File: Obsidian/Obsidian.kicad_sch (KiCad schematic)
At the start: 5 parts

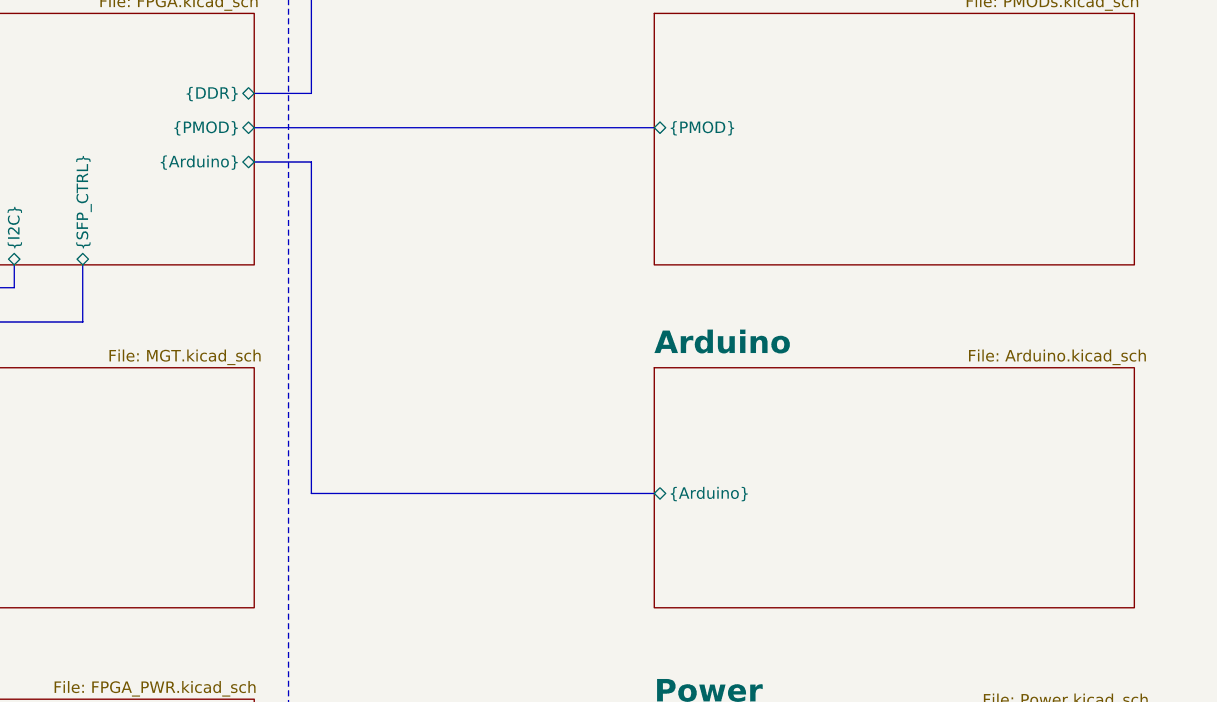
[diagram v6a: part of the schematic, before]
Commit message: adding flex connector
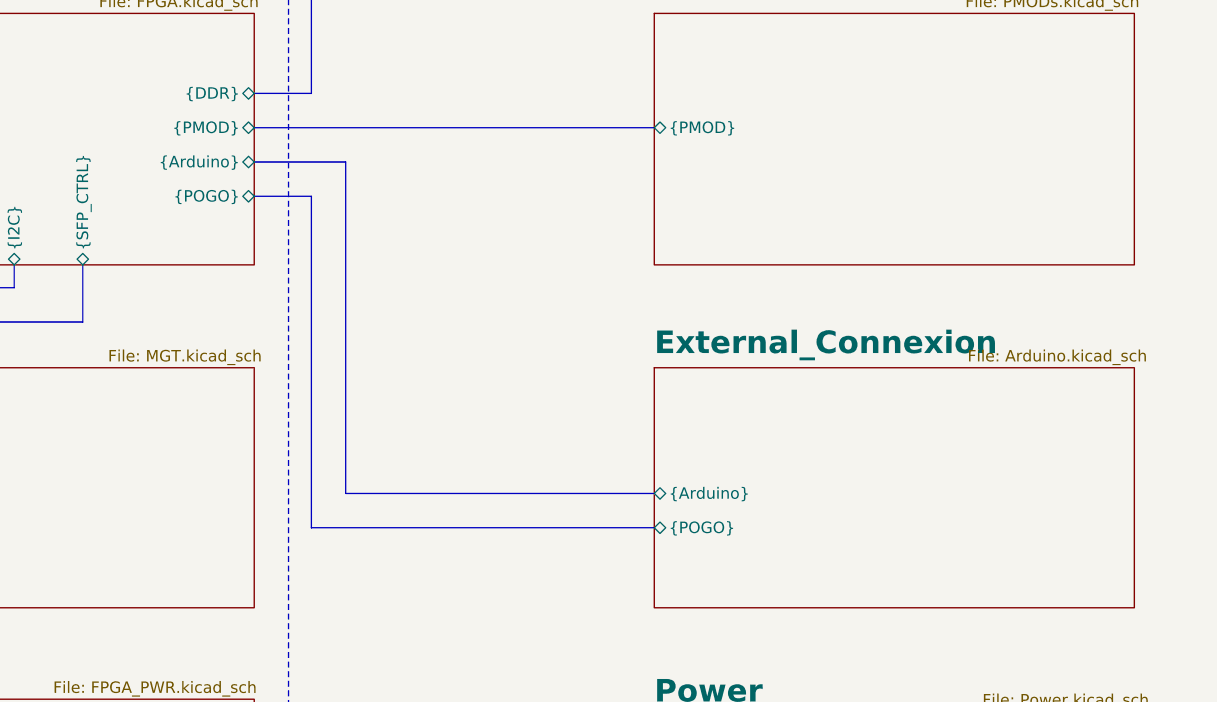
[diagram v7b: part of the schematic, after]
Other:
- sheet Arduino renamed External_Connexion
- sheet External_Connexion ports: added {POGO}; removed none
- sheet FPGA ports: added {POGO}; removed none
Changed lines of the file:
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@@
 	(bus
 		(pts
-			(xy 179.07 110.49) (xy 217.17 110.49)
+			(xy 182.88 110.49) (xy 217.17 110.49)
 		)
 		(stroke
@@
 	(bus
 		(pts
+			(xy 179.07 77.47) (xy 172.72 77.47)
+		)
+		(stroke
+			(width 0)
+			(type default)
+		)
+	)
+	(bus
+		(pts
+			(xy 217.17 114.3) (xy 179.07 114.3)
+		)
+		(stroke
+			(width 0)
+			(type default)
+		)
+	)
+	(bus
+		(pts
 			(xy 114.3 34.29) (xy 114.3 60.96)
 		)
@@
 	(bus
 		(pts
-			(xy 172.72 73.66) (xy 179.07 73.66)
+			(xy 172.72 73.66) (xy 182.88 73.66)
 		)
 		(stroke
@@
 	(bus
 		(pts
-			(xy 179.07 73.66) (xy 179.07 110.49)
+			(xy 182.88 73.66) (xy 182.88 110.49)
 		)
 		(stroke
@@
 		(pts
 			(xy 179.07 31.75) (xy 179.07 66.04)
+		)
+		(stroke
+			(width 0)
+			(type default)
+		)
+	)
+	(bus
+		(pts
+			(xy 179.07 114.3) (xy 179.07 77.47)
 		)
 		(stroke
@@
 			)
 		)
+		(pin "{POGO}" bidirectional
+			(at 172.72 77.47 0)
+			(effects
+				(font
+					(size 1.27 1.27)
+				)
+				(justify right)
+			)
+		)
 		(instances
 			(project "Obsidian"
@@
 			(color 128 255 128 1.0000)
 		)
-		(property "Sheetname" "Arduino"
+		(property "Sheetname" "External_Connexion"
 			(at 217.17 95.1934 0)
 			(effects
@@
 			(effects
 				(font
+					(size 1.27 1.27)
+				)
+				(justify left)
+			)
+		)
+		(pin "{POGO}" bidirectional
+			(at 217.17 114.3 180)
+			(effects
+				(font

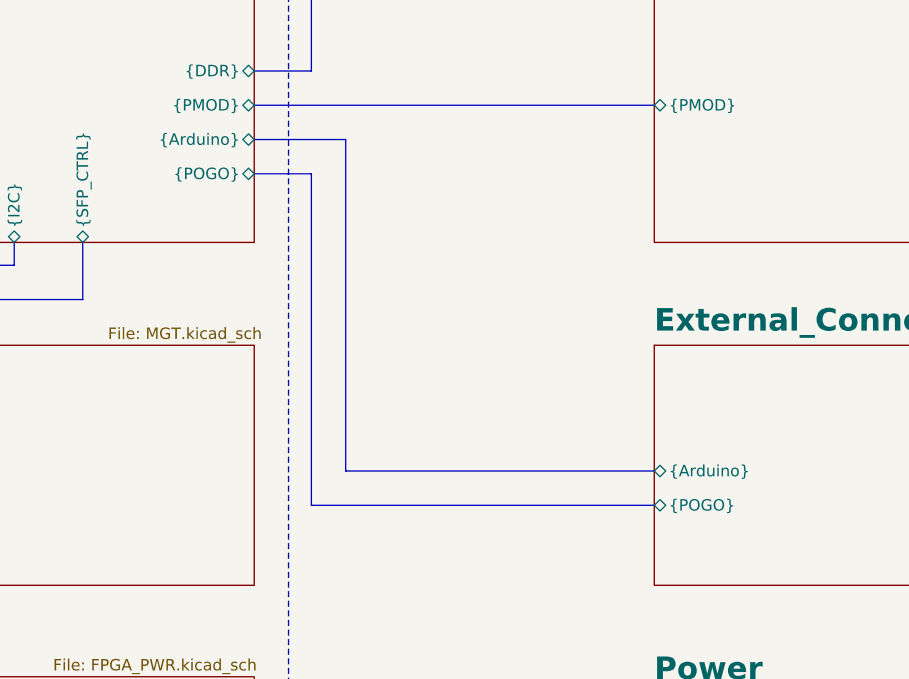
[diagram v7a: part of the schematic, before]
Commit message: Cleanup of the schematic
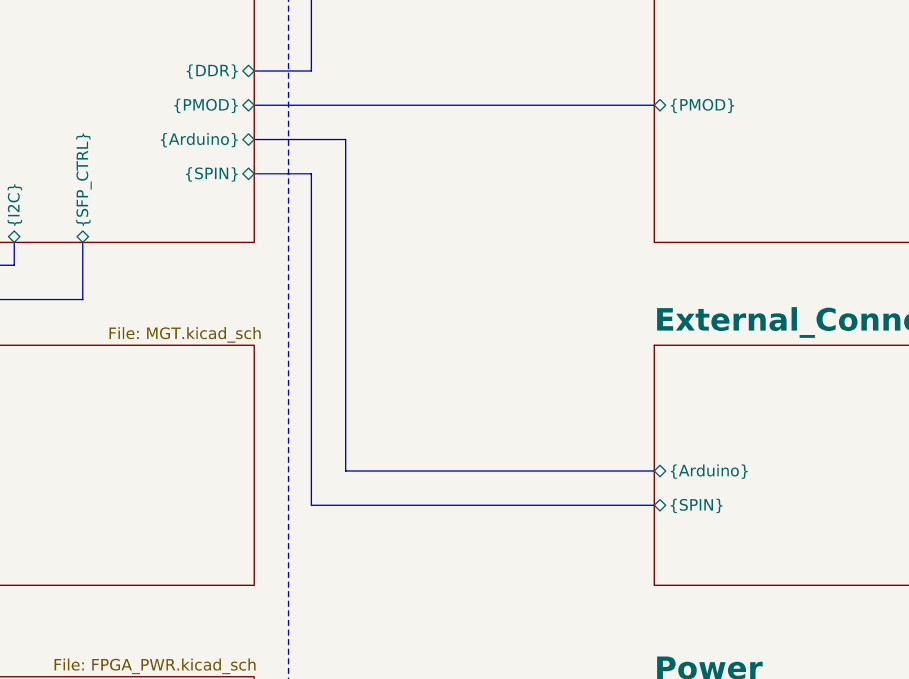
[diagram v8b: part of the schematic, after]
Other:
- sheet External_Connexion ports: added {SPIN}; removed {POGO}
- sheet FPGA ports: added {SPIN}; removed {POGO}
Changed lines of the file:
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@@
 			)
 		)
-		(pin "{POGO}" bidirectional
+		(pin "{SPIN}" bidirectional
 			(at 172.72 77.47 0)
 			(effects
@@
 			)
 		)
-		(pin "{POGO}" bidirectional
+		(pin "{SPIN}" bidirectional
 			(at 217.17 114.3 180)
 			(effects
